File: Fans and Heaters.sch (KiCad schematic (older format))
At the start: 0 parts

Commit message: Started implementing MOSFET drivers
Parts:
- added C? (x2): 0.1uF, symbol Device:C_Small
- added R? (x16): 10k, symbol Device:R_Small_US
- added U? (x2): 74HCT245, symbol MOSFET~Drivers:74HCT245
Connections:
- net labels added: +5V, BED_HEATER, BED_HEATER_BUFF, CHAMBER_HEATER, CHAMBER_HEATER_BUFF, FAN0, FAN0_BUFF, FAN1, FAN1_BUFF, FAN2, FAN2_BUFF, FAN3, FAN3_BUFF, FAN4, FAN4_BUFF, FAN5, FAN5_BUFF, FAN6, FAN6_BUFF, FAN7, FAN7_BUFF, GND, HEATER0, HEATER0_BUFF, HEATER1, HEATER1_BUFF, HEATER2, HEATER2_BUFF, HEATER3, HEATER3_BUFF, HEATER4, HEATER4_BUFF, HEATER5, HEATER5_BUFF
- wire segments 0 -> 118

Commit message: added resistor numbers
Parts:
- gave numbers to parts that had none: 20
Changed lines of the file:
@@
 $EndDescr
 $Comp
-L MOSFET~Drivers:74HCT245 U?
+L MOSFET~Drivers:74HCT245 U5
 U 1 1 5F9B0850
 P 2800 1400
-F 0 "U?" H 2800 1865 50  0000 C CNN
+F 0 "U5" H 2800 1865 50  0000 C CNN
 F 1 "74HCT245" H 2800 1774 50  0000 C CNN
 F 2 "" H 2900 1350 50  0001 C CNN
@@
 $EndComp
 $Comp
-L power:GND #PWR?
+L power:GND #PWR093
 U 1 1 5F9B2E7B
 P 3350 2200
-F 0 "#PWR?" H 3350 1950 50  0001 C CNN
+F 0 "#PWR093" H 3350 1950 50  0001 C CNN
 F 1 "GND" H 3355 2027 50  0000 C CNN
 F 2 "" H 3350 2200 50  0001 C CNN
@@
 $EndComp
 $Comp
-L power:+5V #PWR?
+L power:+5V #PWR091
 U 1 1 5F9B33D5
 P 2150 1100
-F 0 "#PWR?" H 2150 950 50  0001 C CNN
+F 0 "#PWR091" H 2150 950 50  0001 C CNN
 F 1 "+5V" H 2165 1273 50  0000 C CNN
 F 2 "" H 2150 1100 50  0001 C CNN
@@
 $EndComp
 $Comp
-L Device:C_Small C?
+L Device:C_Small C110
 U 1 1 5F9B3948
 P 1850 1200
-F 0 "C?" V 1621 1200 50  0000 C CNN
+F 0 "C110" V 1621 1200 50  0000 C CNN
 F 1 "0.1uF" V 1712 1200 50  0000 C CNN
 F 2 "" H 1850 1200 50  0001 C CNN
@@
 	3350 2100 3350 2000
 $Comp
-L power:GND #PWR?
+L power:GND #PWR089
 U 1 1 5F9B4148
 P 1550 1200
-F 0 "#PWR?" H 1550 950 50  0001 C CNN
+F 0 "#PWR089" H 1550 950 50  0001 C CNN
 F 1 "GND" V 1555 1072 50  0000 R CNN
 F 2 "" H 1550 1200 50  0001 C CNN
@@
 	1550 1200 1750 1200
 $Comp
-L Device:R_Small_US R?
+L Device:R_Small_US R32
 U 1 1 5F9B8835
 P 1550 2300
-F 0 "R?" V 1600 2350 39  0000 L CNN
+F 0 "R32" V 1600 2350 39  0000 L CNN
 F 1 "10k" V 1600 2150 39  0000 L CNN
 F 2 "" H 1550 2300 50  0001 C CNN
@@
 $EndComp
 $Comp
-L Device:R_Small_US R?
+L Device:R_Small_US R30
 U 1 1 5F9B89A0
 P 1450 2300
-F 0 "R?" V 1500 2350 39  0000 L CNN
+F 0 "R30" V 1500 2350 39  0000 L CNN
 F 1 "10k" V 1500 2150 39  0000 L CNN
 F 2 "" H 1450 2300 50  0001 C CNN
@@
 $EndComp
 $Comp
-L power:GND #PWR?
+L power:GND #PWR087
 U 1 1 5F9B8AF4
 P 1450 2550
-F 0 "#PWR?" H 1450 2300 50  0001 C CNN
+F 0 "#PWR087" H 1450 2300 50  0001 C CNN
 F 1 "GND" H 1455 2377 50  0000 C CNN
 F 2 "" H 1450 2550 50  0001 C CNN
@@
 	2150 2400 2150 2500
 $Comp
-L Device:R_Small_US R?
+L Device:R_Small_US R34
 U 1 1 5F9B86C2
 P 1650 2300
-F 0 "R?" V 1700 2350 39  0000 L CNN
+F 0 "R34" V 1700 2350 39  0000 L CNN
 F 1 "10k" V 1700 2150 39  0000 L CNN
 F 2 "" H 1650 2300 50  0001 C CNN
@@
 $EndComp
 $Comp
-L Device:R_Small_US R?
+L Device:R_Small_US R36
 U 1 1 5F9B859C
 P 1750 2300
-F 0 "R?" V 1800 2350 39  0000 L CNN
+F 0 "R36" V 1800 2350 39  0000 L CNN
 F 1 "10k" V 1800 2150 39  0000 L CNN
 F 2 "" H 1750 2300 50  0001 C CNN
@@
 $EndComp
 $Comp
-L Device:R_Small_US R?
+L Device:R_Small_US R38
 U 1 1 5F9B841D
 P 1850 2300
-F 0 "R?" V 1900 2350 39  0000 L CNN
+F 0 "R38" V 1900 2350 39  0000 L CNN
 F 1 "10k" V 1900 2150 39  0000 L CNN
 F 2 "" H 1850 2300 50  0001 C CNN
@@
 $EndComp
 $Comp
-L Device:R_Small_US R?
+L Device:R_Small_US R40
 U 1 1 5F9B832A
 P 1950 2300
-F 0 "R?" V 2000 2350 39  0000 L CNN
+F 0 "R40" V 2000 2350 39  0000 L CNN
 F 1 "10k" V 2000 2150 39  0000 L CNN
 F 2 "" H 1950 2300 50  0001 C CNN
@@
 $EndComp
 $Comp
-L Device:R_Small_US R?
+L Device:R_Small_US R42
 U 1 1 5F9B8277
 P 2050 2300
-F 0 "R?" V 2100 2350 39  0000 L CNN
+F 0 "R42" V 2100 2350 39  0000 L CNN
 F 1 "10k" V 2100 2150 39  0000 L CNN
 F 2 "" H 2050 2300 50  0001 C CNN
@@
 $EndComp
 $Comp
-L Device:R_Small_US R?
+L Device:R_Small_US R44
 U 1 1 5F9B6E11
 P 2150 2300
-F 0 "R?" V 2200 2350 39  0000 L CNN
+F 0 "R44" V 2200 2350 39  0000 L CNN
 F 1 "10k" V 2200 2150 39  0000 L CNN
 F 2 "" H 2150 2300 50  0001 C CNN
@@
 	3450 1200 3250 1200
 $Comp
-L MOSFET~Drivers:74HCT245 U?
+L MOSFET~Drivers:74HCT245 U6
 U 1 1 5FA09D3F
 P 2800 3350
-F 0 "U?" H 2800 3815 50  0000 C CNN
+F 0 "U6" H 2800 3815 50  0000 C CNN
 F 1 "74HCT245" H 2800 3724 50  0000 C CNN
 F 2 "" H 2900 3300 50  0001 C CNN
@@
 $EndComp
 $Comp
-L power:GND #PWR?
+L power:GND #PWR094
 U 1 1 5FA09D45
 P 3350 4150
-F 0 "#PWR?" H 3350 3900 50  0001 C CNN
+F 0 "#PWR094" H 3350 3900 50  0001 C CNN
 F 1 "GND" H 3355 3977 50  0000 C CNN
 F 2 "" H 3350 4150 50  0001 C CNN
@@
 $EndComp
 $Comp
-L power:+5V #PWR?
+L power:+5V #PWR092
 U 1 1 5FA09D4B
 P 2150 3050
-F 0 "#PWR?" H 2150 2900 50  0001 C CNN
+F 0 "#PWR092" H 2150 2900 50  0001 C CNN
 F 1 "+5V" H 2165 3223 50  0000 C CNN
 F 2 "" H 2150 3050 50  0001 C CNN
@@
 $EndComp
 $Comp
-L Device:C_Small C?
+L Device:C_Small C111
 U 1 1 5FA09D51
 P 1850 3150
-F 0 "C?" V 1621 3150 50  0000 C CNN
+F 0 "C111" V 1621 3150 50  0000 C CNN
 F 1 "0.1uF" V 1712 3150 50  0000 C CNN
 F 2 "" H 1850 3150 50  0001 C CNN
@@
 	3350 4050 3350 3950
 $Comp
-L power:GND #PWR?
+L power:GND #PWR090
 U 1 1 5FA09D60
 P 1550 3150
-F 0 "#PWR?" H 1550 2900 50  0001 C CNN
+F 0 "#PWR090" H 1550 2900 50  0001 C CNN
 F 1 "GND" V 1555 3022 50  0000 R CNN
 F 2 "" H 1550 3150 50  0001 C CNN
@@
 	1550 3150 1750 3150
 $Comp
-L Device:R_Small_US R?
+L Device:R_Small_US R33
 U 1 1 5FA09D67
 P 1550 4250
-F 0 "R?" V 1600 4300 39  0000 L CNN
+F 0 "R33" V 1600 4300 39  0000 L CNN
 F 1 "10k" V 1600 4100 39  0000 L CNN
 F 2 "" H 1550 4250 50  0001 C CNN
@@
 $EndComp
 $Comp
-L Device:R_Small_US R?
+L Device:R_Small_US R31
 U 1 1 5FA09D6D
 P 1450 4250
-F 0 "R?" V 1500 4300 39  0000 L CNN
+F 0 "R31" V 1500 4300 39  0000 L CNN
 F 1 "10k" V 1500 4100 39  0000 L CNN
 F 2 "" H 1450 4250 50  0001 C CNN
@@
 $EndComp
 $Comp
-L power:GND #PWR?
+L power:GND #PWR088
 U 1 1 5FA09D73
 P 1450 4500
-F 0 "#PWR?" H 1450 4250 50  0001 C CNN
+F 0 "#PWR088" H 1450 4250 50  0001 C CNN
 F 1 "GND" H 1455 4327 50  0000 C CNN
 F 2 "" H 1450 4500 50  0001 C CNN
@@
 	2150 4350 2150 4450
 $Comp
-L Device:R_Small_US R?
+L Device:R_Small_US R35
 U 1 1 5FA09D9C
 P 1650 4250
-F 0 "R?" V 1700 4300 39  0000 L CNN
+F 0 "R35" V 1700 4300 39  0000 L CNN
 F 1 "10k" V 1700 4100 39  0000 L CNN
 F 2 "" H 1650 4250 50  0001 C CNN
@@
 $EndComp
 $Comp
-L Device:R_Small_US R?
+L Device:R_Small_US R37
 U 1 1 5FA09DA2
 P 1750 4250
-F 0 "R?" V 1800 4300 39  0000 L CNN
+F 0 "R37" V 1800 4300 39  0000 L CNN
 F 1 "10k" V 1800 4100 39  0000 L CNN
 F 2 "" H 1750 4250 50  0001 C CNN
@@
 $EndComp
 $Comp
-L Device:R_Small_US R?
+L Device:R_Small_US R39
 U 1 1 5FA09DA8
 P 1850 4250
-F 0 "R?" V 1900 4300 39  0000 L CNN
+F 0 "R39" V 1900 4300 39  0000 L CNN
 F 1 "10k" V 1900 4100 39  0000 L CNN
 F 2 "" H 1850 4250 50  0001 C CNN
@@
 $EndComp
 $Comp
-L Device:R_Small_US R?
+L Device:R_Small_US R41
 U 1 1 5FA09DAE
 P 1950 4250
-F 0 "R?" V 2000 4300 39  0000 L CNN
+F 0 "R41" V 2000 4300 39  0000 L CNN
 F 1 "10k" V 2000 4100 39  0000 L CNN
 F 2 "" H 1950 4250 50  0001 C CNN
@@
 $EndComp
 $Comp
-L Device:R_Small_US R?
+L Device:R_Small_US R43
 U 1 1 5FA09DB4
 P 2050 4250
-F 0 "R?" V 2100 4300 39  0000 L CNN
+F 0 "R43" V 2100 4300 39  0000 L CNN
 F 1 "10k" V 2100 4100 39  0000 L CNN
 F 2 "" H 2050 4250 50  0001 C CNN
@@
 $EndComp
 $Comp
-L Device:R_Small_US R?
+L Device:R_Small_US R45
 U 1 1 5FA09DBA
 P 2150 4250
-F 0 "R?" V 2200 4300 39  0000 L CNN
+F 0 "R45" V 2200 4300 39  0000 L CNN
 F 1 "10k" V 2200 4100 39  0000 L CNN
 F 2 "" H 2150 4250 50  0001 C CNN

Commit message: added MOSFETs schematic for fans and heaters.
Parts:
- added D? (x16): Schottky, symbol Device:D_Schottky
- added D? (x8): LED, symbol Device:LED_Small
- added J?: H0, symbol Connector_Generic:Conn_01x02
- added J?: H1, symbol Connector_Generic:Conn_01x02
- added J?: H2, symbol Connector_Generic:Conn_01x02
- added J?: H3, symbol Connector_Generic:Conn_01x02
- added J?: H4, symbol Connector_Generic:Conn_01x02
- added J?: H5, symbol Connector_Generic:Conn_01x02
- added J?: HC, symbol Connector_Generic:Conn_01x02
- added J?: HB, symbol Connector_Generic:Conn_01x02
- added J?: F0, symbol Connector_Generic:Conn_01x02
- added J?: F1, symbol Connector_Generic:Conn_01x02
- added J?: F2, symbol Connector_Generic:Conn_01x02
- added J?: F3, symbol Connector_Generic:Conn_01x02
- added J? (x8): Conn_02x03_Odd_Even, symbol Connector_Generic:Conn_02x03_Odd_Even
- added J?: F4, symbol Connector_Generic:Conn_01x02
- added J?: F5, symbol Connector_Generic:Conn_01x02
- added J?: F6, symbol Connector_Generic:Conn_01x02
- added J?: F7, symbol Connector_Generic:Conn_01x02
- added Q? (x16): Q_NMOS_GDS, symbol Device:Q_NMOS_GDS
- added R? (x16): 100, symbol Device:R_Small_US
- added R? (x8): 2.2k, symbol Device:R_Small_US
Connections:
- net labels added: +12V, VIN_BED_FUSED, VIN_FUSED
- wire segments 118 -> 454
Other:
- note added: "Add fusing to heater outputs?\n"

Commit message: added raspberry pi header
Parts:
- gave numbers to parts that had none: 88

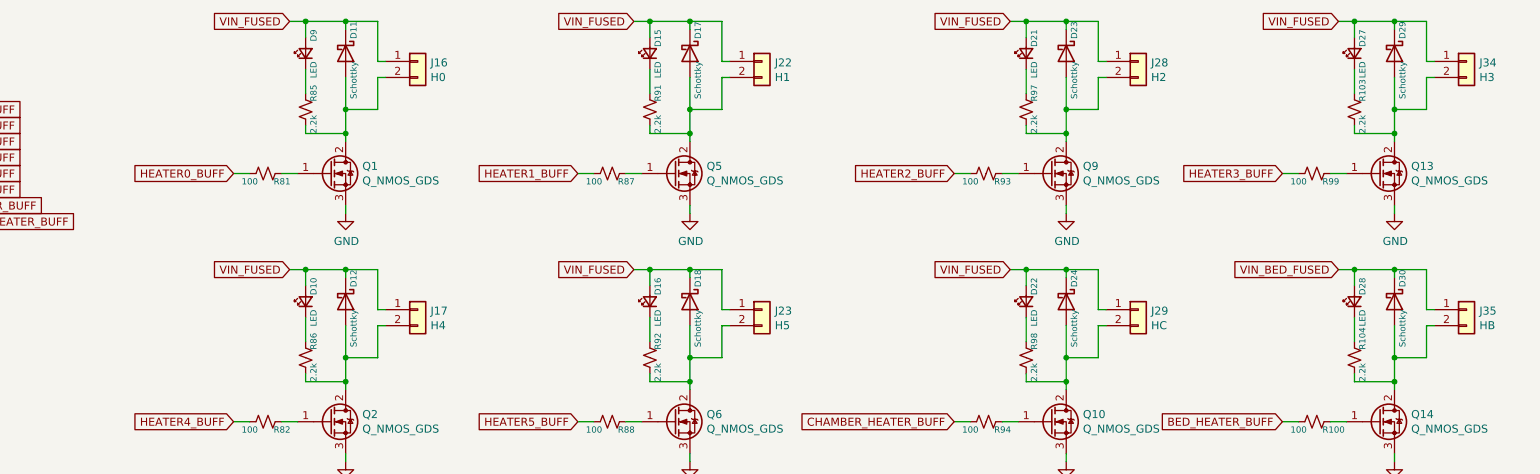
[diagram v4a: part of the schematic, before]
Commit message: associated more footprints
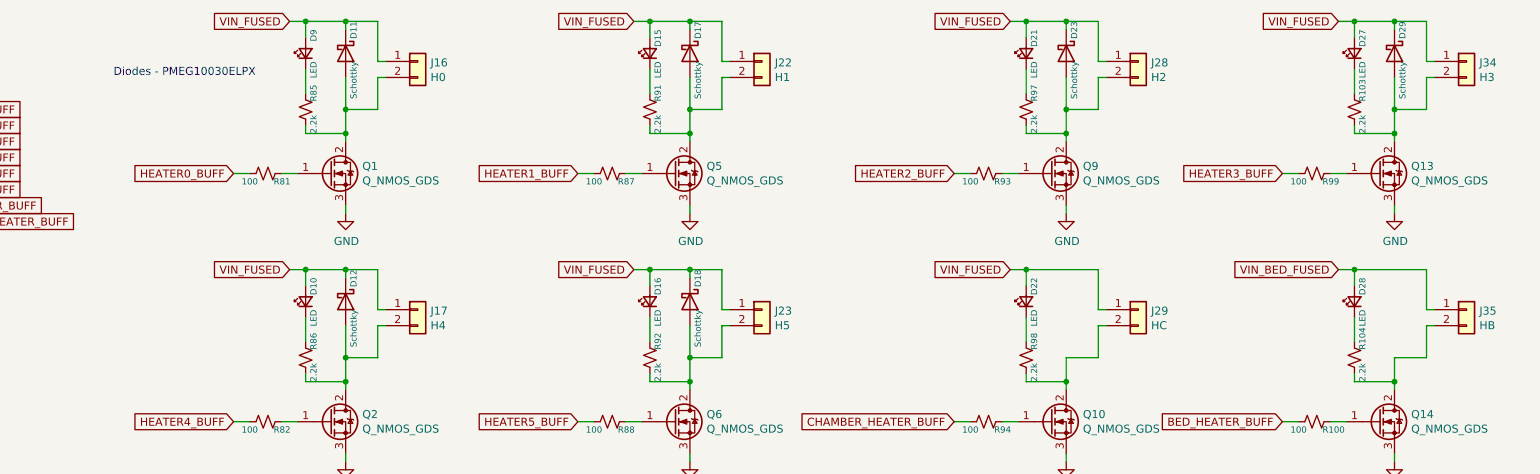
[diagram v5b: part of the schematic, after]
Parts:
- removed D24, D30: Schottky, symbol Device:D_Schottky
- C110, C111: footprint (none) -> Capacitor_SMD:C_0603_1608Metric_Pad1.05x0.95mm_HandSolder
- D10, D15, D16, D21, D22, D27, D28, D9: footprint (none) -> LED_SMD:LED_0603_1608Metric_Pad1.05x0.95mm_HandSolder
- D11, D12, D13, D14, D17, D18, D19, D20, D23, D25, D26, D29, D31, D32: footprint (none) -> Diode_SMD:D_SOD-128
- J14, J15, J20, J21, J26, J27, J32, J33: footprint (none) -> Connector_PinHeader_2.54mm:PinHeader_2x03_P2.54mm_Vertical
- J18, J19, J24, J25, J30, J31, J36, J37: footprint (none) -> Connector_Molex:Molex_KK-254_AE-6410-02A_1x02_P2.54mm_Vertical
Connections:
- wire segments 454 -> 448
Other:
- note added: "Diodes - PMEG10030ELPX"

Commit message: Added more footprints
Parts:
- R100, R101, R102, R103, R104, R30, R31, R32, R33, R34, R35, R36, R37, R38, R39, R40, R41, R42, R43, R44, R45, R81, R82, R83, R84, R85, R86, R87, R88, R89, R90, R91, R92, R93, R94, R95, R96, R97, R98, R99: footprint (none) -> Resistor_SMD:R_0603_1608Metric_Pad1.05x0.95mm_HandSolder
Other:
- note added: "RNCP0603FTD681R"

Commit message: finished associating footprints with symbols
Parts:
- removed Q11, Q12, Q15, Q16, Q3, Q4, Q7, Q8: Q_NMOS_GDS, symbol Device:Q_NMOS_GDS
- removed U5, U6: 74HCT245, symbol MOSFET~Drivers:74HCT245
- added Q11, Q12, Q15, Q16, Q3, Q4, Q7, Q8: Q_NMOS_GSD, Package_TO_SOT_SMD:SOT-23_Handsoldering, symbol Device:Q_NMOS_GSD
- added U5, U6: 74HCT245, Package_SO:SO-20_12.8x7.5mm_P1.27mm, symbol MOSFET_Drivers:74HCT245
- J16, J17, J22, J23, J28, J34: footprint (none) -> TerminalBlock_Phoenix:TerminalBlock_Phoenix_MKDS-1,5-2_1x02_P5.00mm_Horizontal
- J29, J35: footprint (none) -> TerminalBlock_Dinkle:TerminalBlock_Dinkle_DT-55-B01X-02_P10.00mm
- Q1, Q10, Q13, Q14, Q2, Q5, Q6, Q9: footprint (none) -> Package_TO_SOT_SMD:TO-252-2
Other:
- note added: "Bed and Chamber - IPD036N04L"
- note added: "Fan mosfets - CSD18532"
- note added: "Hotends - AOD4184A"
- note added: "Specific model - 74HC245D\nuses SO20 package\n"

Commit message: started initial layout
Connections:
- net VIN_BED_FUSED: now also D22.2 (A), J29.1 (Pin_1)
- net VIN_FUSED: no longer D22.2 (A), J29.1 (Pin_1)
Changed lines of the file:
@@
 Wire Wire Line
 	12050 3150 11950 3150
-Text GLabel 10250 2200 0    50   Input ~ 0
-VIN_FUSED
 $Comp
 L Device:LED_Small D28
@@
 Text Notes 2350 2700 0    50   ~ 0
 Specific model - 74HC245D\nuses SO20 package\n
+Text GLabel 10250 2200 0    50   Input ~ 0
+VIN_BED_FUSED
 $EndSCHEMATC
